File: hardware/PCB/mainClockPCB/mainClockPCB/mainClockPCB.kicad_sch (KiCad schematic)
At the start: 54 parts, among them IC1 ESP32-S3-WROOM-1-N16R2, IC2 SPX1117M3-L_TR, IC3 MCP7940N-I_P, IC4 PAM8904QJER, J1 USB_C_Receptacle_USB2.0_16P, J2 Conn_01x09_Socket, J3 Conn_01x02_Socket, SW1 SW_Push, SW2 SW_Push, SW3 SW_Push, SW4 SW_Push, SW5 SW_Push, SW6 SW_Push, SW7 SW_Push, SW8 SW_Push, SW9 SW_Push, U1 PEC11R-4320K-S0012, U2 USBLC6-2SC6, U3 ESP32-S3-WROOM-2, Y1 AB26T-32.768KHZ-6

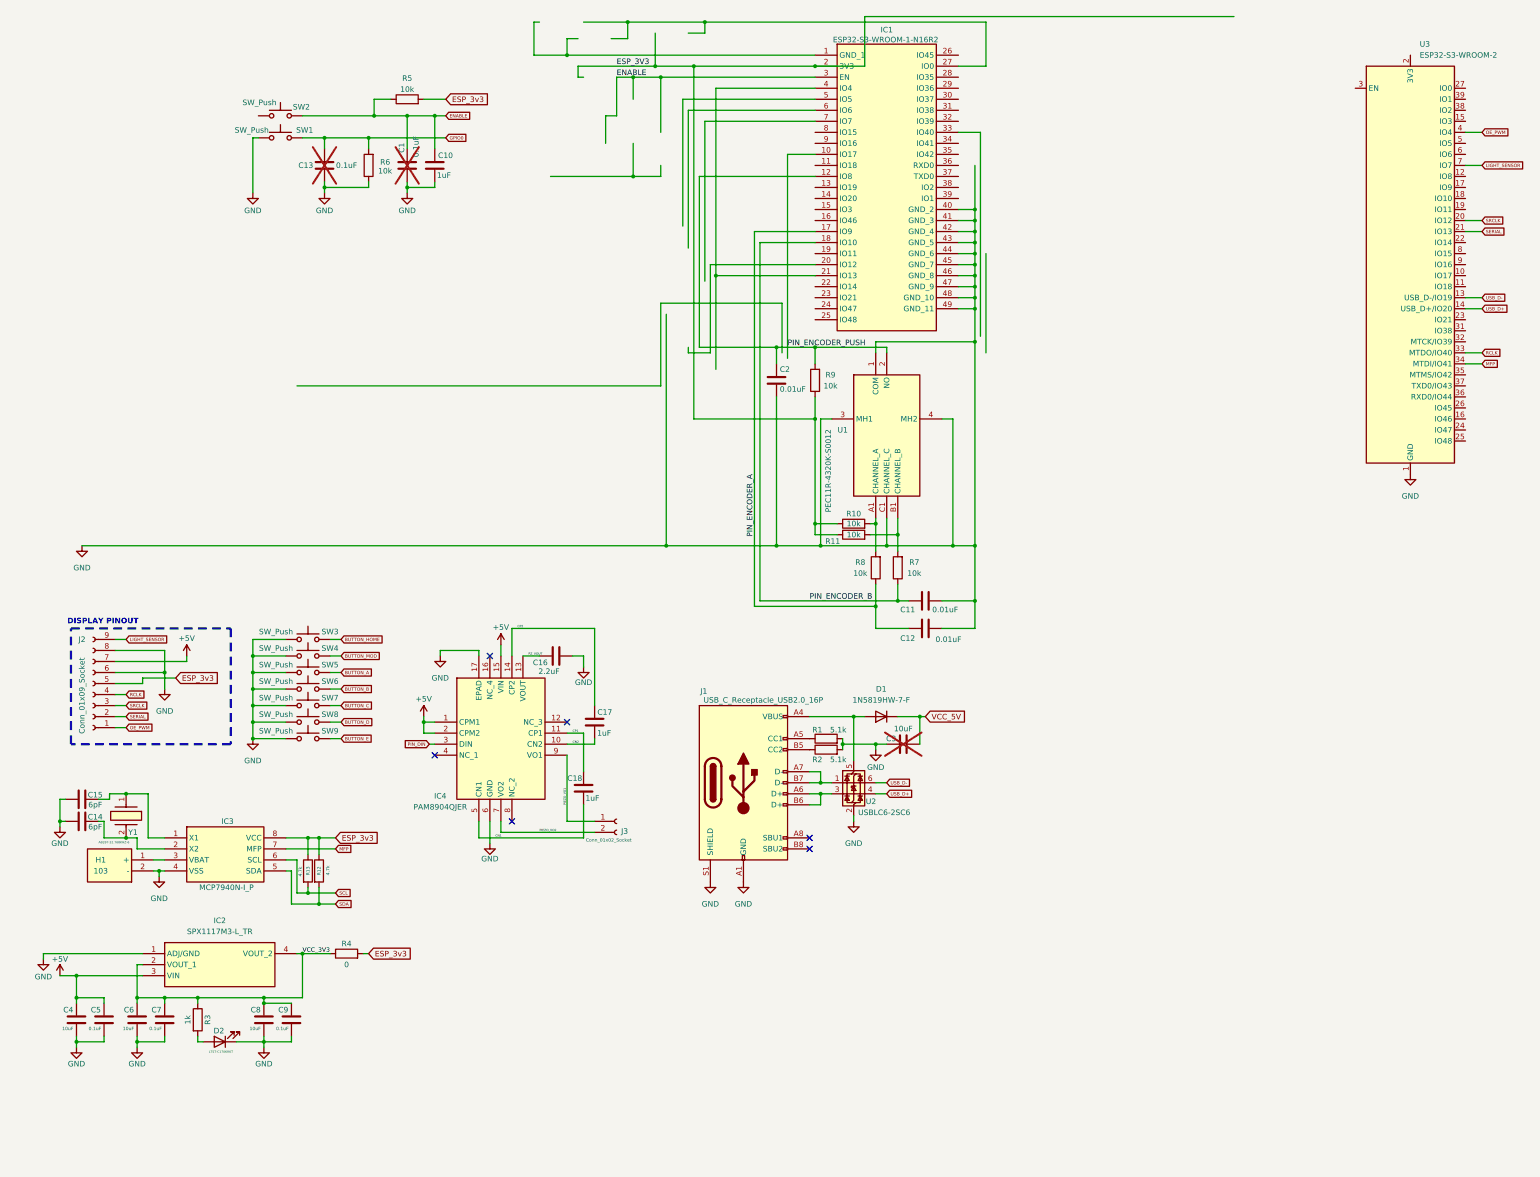
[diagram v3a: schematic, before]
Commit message: encoder schema cleanup
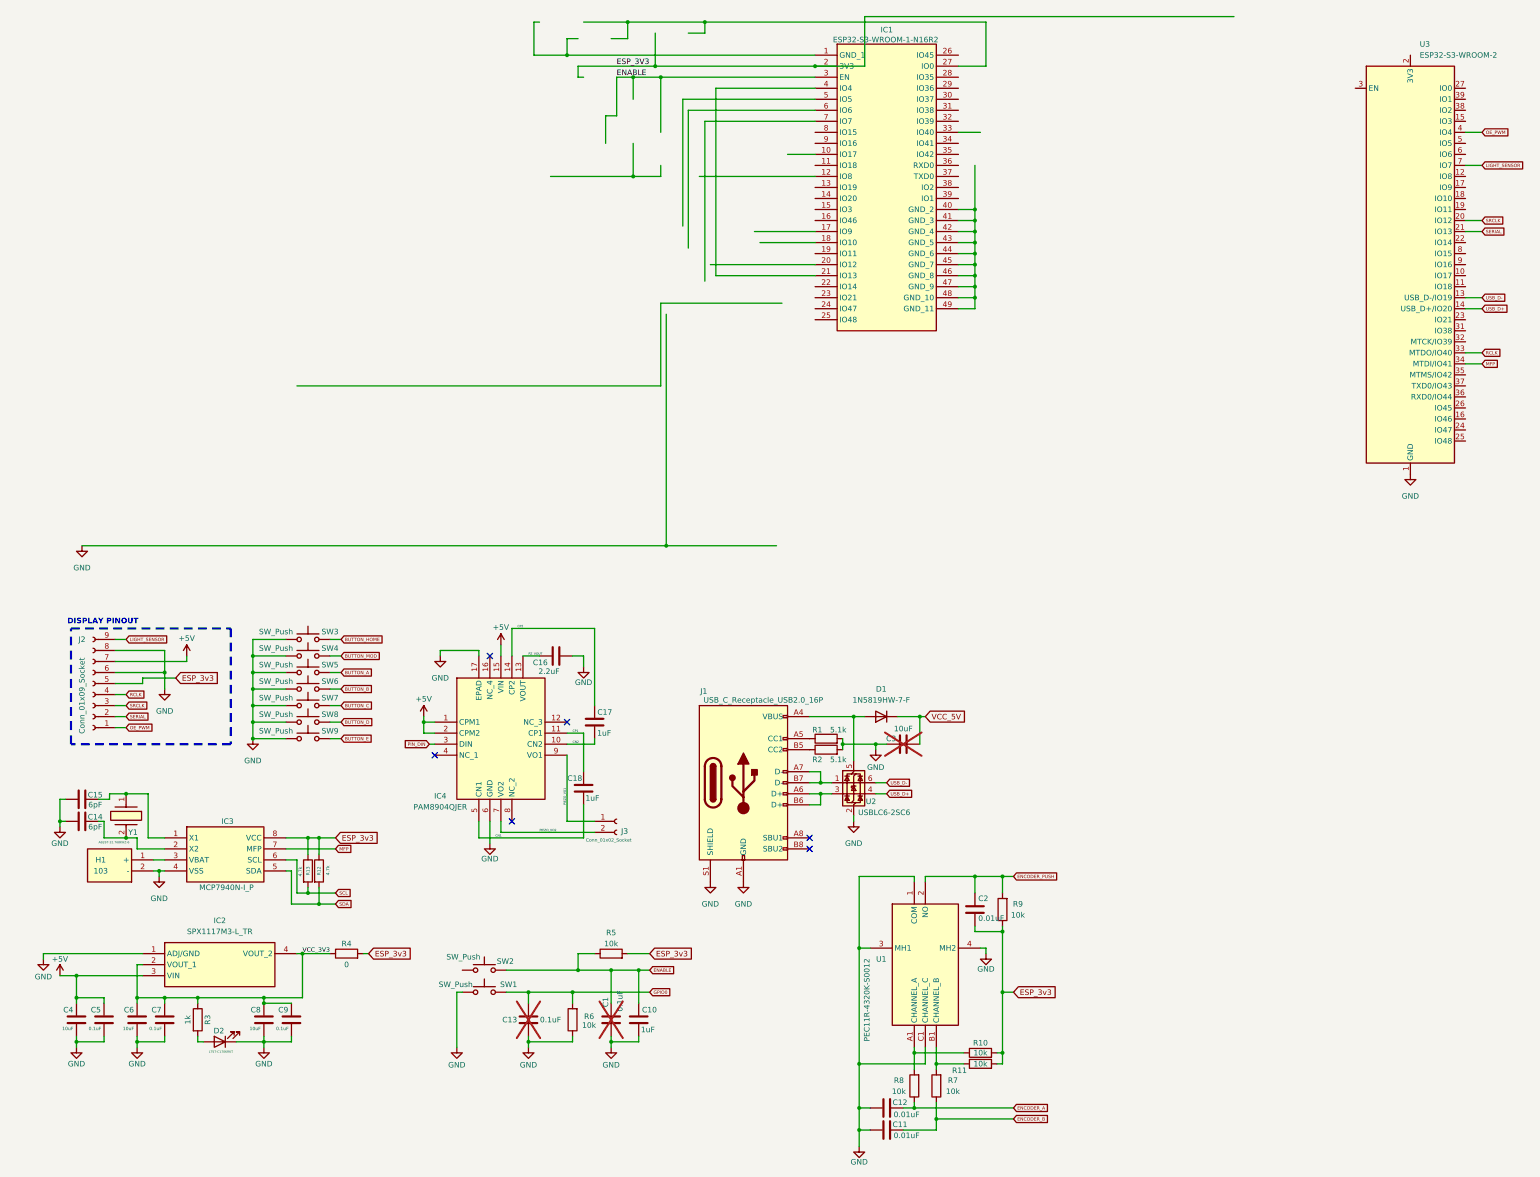
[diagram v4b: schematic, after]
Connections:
- net ESP_3V3: no longer R10.1, R11.1, R9.1
- net ESP_3v3: now also C2.2, R10.2, R11.2, R9.1
- net GND: now also C12.1; no longer C12.2, C2.2, IC1.40 (GND_2), IC1.41 (GND_3), IC1.42 (GND_4), IC1.43 (GND_5), IC1.44 (GND_6), IC1.45 (GND_7), IC1.46 (GND_8), IC1.47 (GND_9), IC1.48 (GND_10), IC1.49 (GND_11)
- net at R7.2, U1.B1 (CHANNEL_B): now also R11.1; no longer R11.2
- net at R8.2, U1.A1 (CHANNEL_A): now also R10.1; no longer R10.2
- removed net PIN_ENCODER_A: C12.1, IC1.17 (IO9), R8.1
- net PIN_ENCODER_B renamed ENCODER_B
- net ENCODER_B: no longer IC1.18 (IO10)
- net PIN_ENCODER_PUSH renamed ENCODER_PUSH
- net ENCODER_PUSH: no longer IC1.10 (IO17), IC1.12 (IO8)
- new net: IC1.40 (GND_2), IC1.41 (GND_3), IC1.42 (GND_4), IC1.43 (GND_5), IC1.44 (GND_6), IC1.45 (GND_7), IC1.46 (GND_8), IC1.47 (GND_9), IC1.48 (GND_10), IC1.49 (GND_11)
- new net ENCODER_A: C12.2, R8.1
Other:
- moved on the sheet: C1, C10, C11, C12, C13, C2, R10, R11, R5, R6, R7, R8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

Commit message: ESP32 schema cleanup
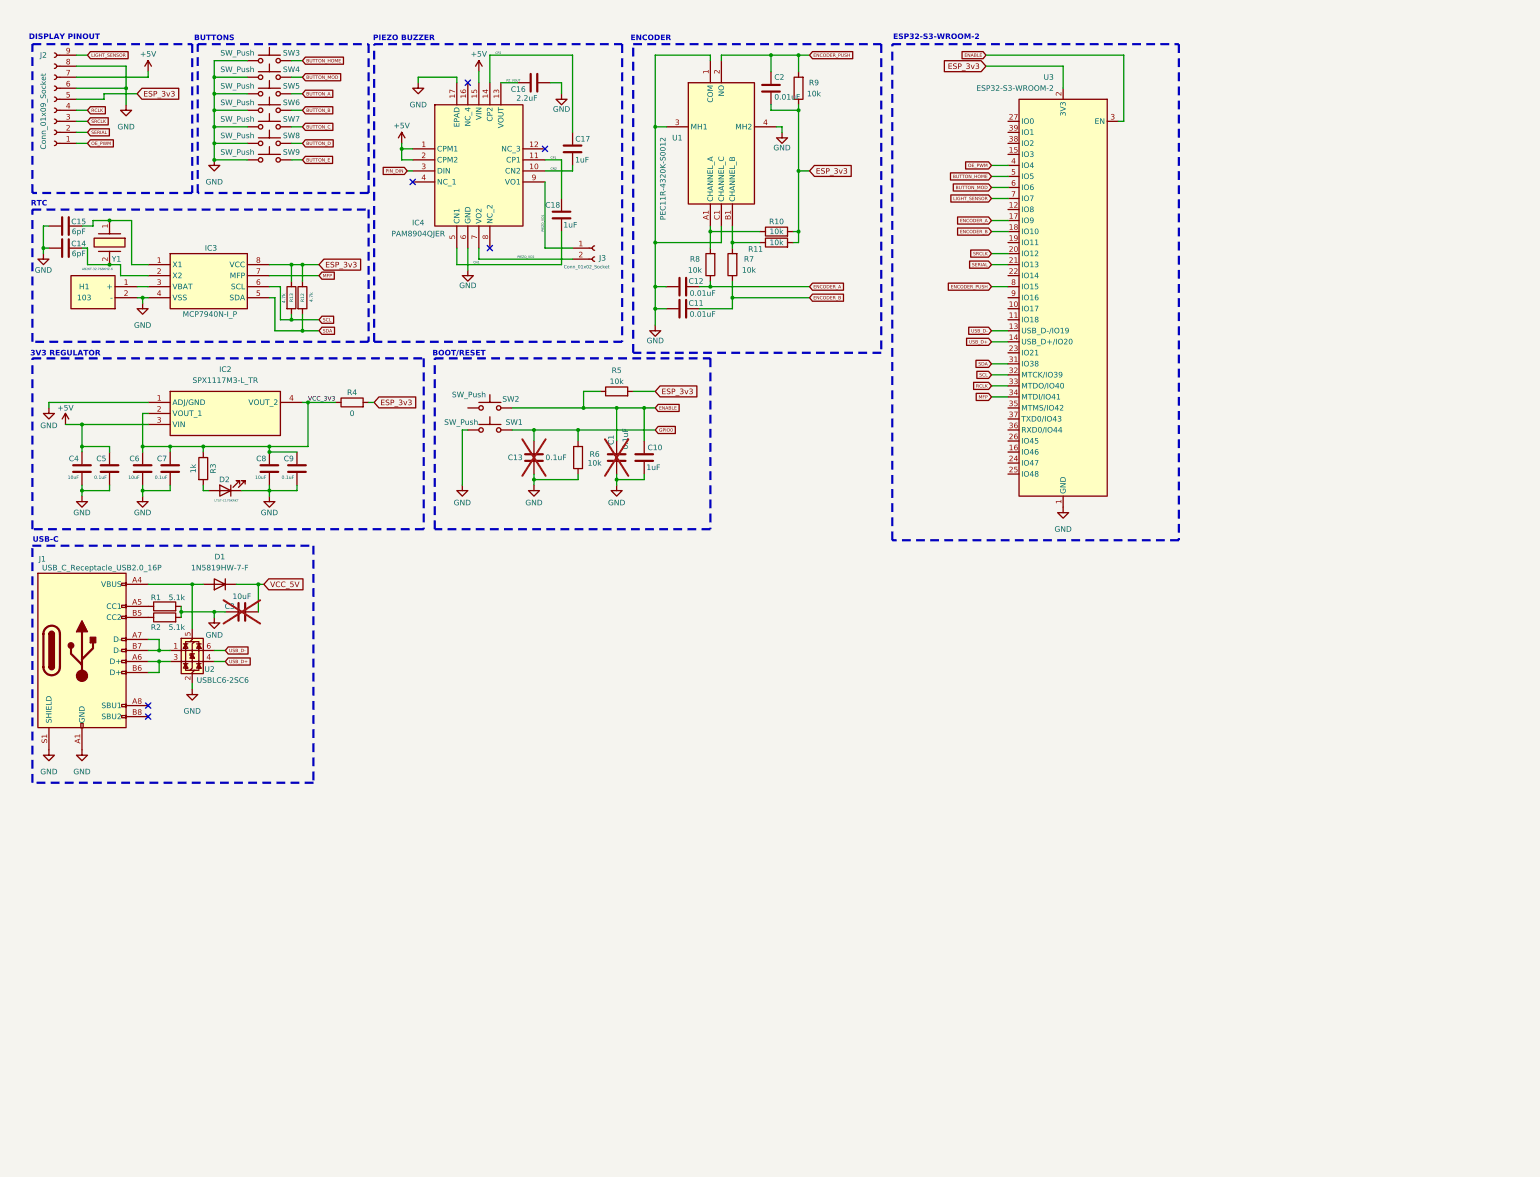
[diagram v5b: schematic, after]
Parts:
- removed IC1: ESP32-S3-WROOM-1-N16R2, SamacSys_Parts:ESP32S3WROOM1N16R2, symbol SamacSys_Parts:ESP32-S3-WROOM-1-N16R2
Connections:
- net BUTTON_HOME: now also U3.5 (IO5)
- net BUTTON_MOD: now also U3.6 (IO6)
- net ENABLE: now also U3.3 (EN)
- net ENCODER_A: now also U3.17 (IO9)
- net ENCODER_B: now also U3.18 (IO10)
- net ENCODER_PUSH: now also U3.8 (IO15)
- net ESP_3v3: now also U3.2 (3V3)
- net SCL: now also U3.32 (MTCK/IO39)
- net SDA: now also U3.31 (IO38)
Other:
- note added: "3V3 REGULATOR"
- note added: "BOOT/RESET"
- note added: "BUTTONS"
- note added: "ENCODER"
- note added: "ESP32-S3-WROOM-2"
- note added: "PIEZO BUZZER"
- note added: "RTC"
- note added: "USB-C"
- title: (none) -> ESP32 CLOCK MAIN BOARD
- moved on the sheet: C1, C10, C11, C12, C13, C14, C15, C16, C17, C18, C2, C3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
